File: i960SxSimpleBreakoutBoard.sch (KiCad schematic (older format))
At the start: 26 parts, among them J1 Conn_01x07, J2 Pure Input Pins, J3 Clock, Power, and Bidirection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, J4 Conn_01x05, J5 Multiplexed Address/Data Lines, J6 Upper 16 Address Lines, U1 80960Sx

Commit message: go with a single 1 row connector for the right side of the design
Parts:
- removed J2: Pure Input Pins, Connector_PinHeader_2.54mm:PinHeader_2x03_P2.54mm_Vertical, symbol Connector_Generic:Conn_02x03_Counter_Clockwise
- added J?: Conn_01x11, symbol Connector_Generic:Conn_01x11
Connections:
- net HOLD: now also J?.2 (Pin_2)
- net INT1: now also J?.5 (Pin_5)
- net INT2: now also J?.4 (Pin_4)
- net ~INT0: now also J?.6 (Pin_6)
- net ~INT3: now also J?.3 (Pin_3); no longer J3.5 (Pin_5)
- net ~READY: now also J?.1 (Pin_1)
- net ~RESET: now also J?.7 (Pin_7)
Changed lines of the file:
@@
 Wire Wire Line
 	10650 3450 10950 3450
-Text Label 10950 3550 0    50   ~ 0
+Text Label 11450 2100 0    50   ~ 0
 ~INT3
 Text Label 10950 3450 0    50   ~ 0
@@
 ALE
 Wire Wire Line
-	9600 2400 10100 2400
-Wire Wire Line
-	9600 2500 10100 2500
-Text Label 9600 2400 0    50   ~ 0
+	11450 1900 11950 1900
+Wire Wire Line
+	11450 2000 11950 2000
+Text Label 11450 1900 0    50   ~ 0
 ~READY
 Text Label 6550 4100 0    50   ~ 0
@@
 Text Label 6600 4200 0    50   ~ 0
 HOLD
-Text Label 9600 2500 0    50   ~ 0
+Text Label 11450 2000 0    50   ~ 0
 HOLD
 Wire Wire Line
@@
 Text Label 8200 4500 0    50   ~ 0
 ~RESET
-Text Label 9600 2600 0    50   ~ 0
+Text Label 11450 2500 0    50   ~ 0
 ~RESET
 Wire Wire Line
-	9600 2600 10100 2600
-Text Label 11100 2600 2    50   ~ 0
+	11450 2500 11950 2500
+Text Label 11450 2400 0    50   ~ 0
 ~INT0
-Text Label 11100 2500 2    50   ~ 0
+Text Label 11450 2300 0    50   ~ 0
 INT1
-Text Label 11100 2400 2    50   ~ 0
+Text Label 11450 2200 0    50   ~ 0
 INT2
 Wire Wire Line
-	11100 2600 10600 2600
-Wire Wire Line
-	11100 2500 10600 2500
-Wire Wire Line
-	11100 2400 10600 2400
+	11450 2400 11950 2400
+Wire Wire Line
+	11450 2300 11950 2300
+Wire Wire Line
+	11450 2200 11950 2200
 $Comp
 L power:GND #PWR08
@@
 Wire Wire Line
 	10350 5550 10850 5550
-$Comp
-L Connector_Generic:Conn_02x03_Counter_Clockwise J2
-U 1 1 60272919
-P 10300 2500
-F 0 "J2" H 10350 2817 50  0000 C CNN
-F 1 "Pure Input Pins" H 10350 2726 50  0000 C CNN
-F 2 "Connector_PinHeader_2.54mm:PinHeader_2x03_P2.54mm_Vertical" H 10300 2500 50  0001 C CNN
-F 3 "~" H 10300 2500 50  0001 C CNN
-	1    10300 2500
-	1    0    0    -1
-$EndComp
 $Comp
 L Connector_Generic:Conn_02x03_Counter_Clockwise J3
@@
 $EndComp
 NoConn ~ 13950 3500
+$Comp
+L Connector_Generic:Conn_01x11 J?
+U 1 1 5FBBE5ED
+P 12150 2400
+F 0 "J?" H 12230 2442 50  0000 L CNN
+F 1 "Conn_01x11" H 12230 2351 50  0000 L CNN
+F 2 "" H 12150 2400 50  0001 C CNN
+F 3 "~" H 12150 2400 50  0001 C CNN
+	1    12150 2400
+	1    0    0    -1
+$EndComp
+Wire Wire Line
+	11450 2100 11950 2100
 $EndSCHEMATC

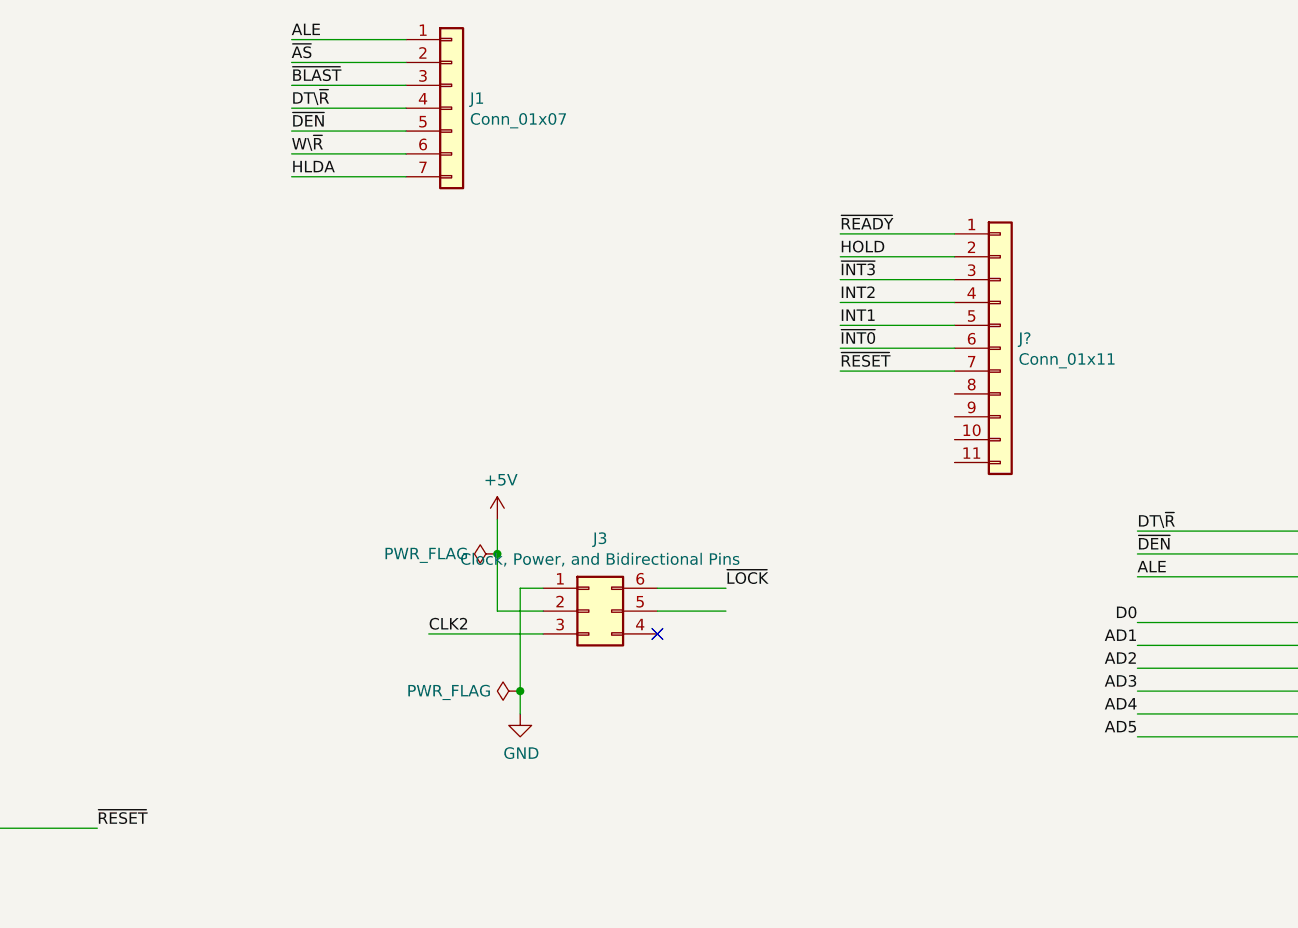
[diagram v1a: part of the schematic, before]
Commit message: Shrunk the size of the final pcb
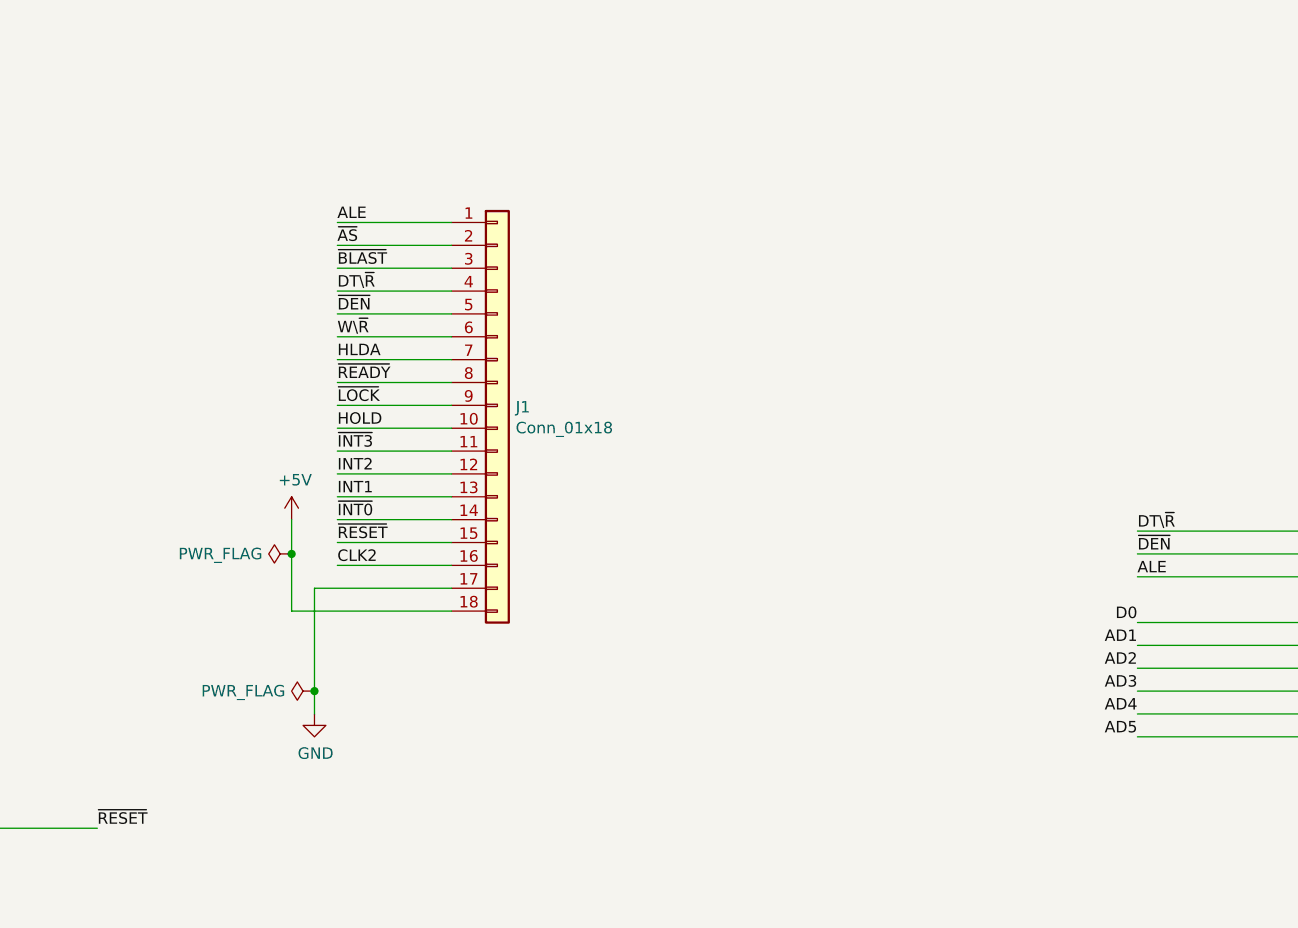
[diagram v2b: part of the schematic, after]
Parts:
- removed J1: Conn_01x07, Connector_PinHeader_2.54mm:PinHeader_1x07_P2.54mm_Vertical, symbol Connector_Generic:Conn_01x07
- removed J3: Clock, Power, and Bidirectional Pins, Connector_PinHeader_2.54mm:PinHeader_2x03_P2.54mm_Vertical, symbol Connector_Generic:Conn_02x03_Counter_Clockwise
- removed J?: Conn_01x11, symbol Connector_Generic:Conn_01x11
- added J1: Conn_01x18, Connector_PinHeader_2.54mm:PinHeader_1x18_P2.54mm_Vertical, symbol Connector_Generic:Conn_01x18
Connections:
- net +5V: now also J1.18 (Pin_18)
- net ALE: now also J1.1 (Pin_1)
- net CLK2: now also J1.16 (Pin_16)
- net DT\~R: now also J1.4 (Pin_4)
- net GND: now also J1.17 (Pin_17)
- net HLDA: now also J1.7 (Pin_7)
- net HOLD: now also J1.10 (Pin_10)
- net INT1: now also J1.13 (Pin_13)
- net INT2: now also J1.12 (Pin_12)
- net W\~R: now also J1.6 (Pin_6)
- net ~AS: now also J1.2 (Pin_2)
- net ~BLAST: now also J1.3 (Pin_3)
- net ~DEN: now also J1.5 (Pin_5)
- net ~INT0: now also J1.14 (Pin_14)
- net ~INT3: now also J1.11 (Pin_11)
- net ~LOCK: now also J1.9 (Pin_9)
- net ~READY: now also J1.8 (Pin_8)
- net ~RESET: now also J1.15 (Pin_15)
- no-connect marks 2 -> 1
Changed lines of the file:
@@
 BA1
 Wire Wire Line
-	9550 1550 9050 1550
-Wire Wire Line
-	9550 1250 9050 1250
-Wire Wire Line
-	9550 1350 9050 1350
-Wire Wire Line
-	9550 1450 9050 1450
-Text Label 9050 1250 0    50   ~ 0
+	9750 2350 9250 2350
+Wire Wire Line
+	9750 2050 9250 2050
+Wire Wire Line
+	9750 2150 9250 2150
+Wire Wire Line
+	9750 2250 9250 2250
+Text Label 9250 2050 0    50   ~ 0
 ~BLAST
-Text Label 9050 1650 0    50   ~ 0
+Text Label 9250 2450 0    50   ~ 0
 HLDA
 Wire Wire Line
@@
 	10350 5450 10850 5450
 Wire Wire Line
-	9050 1650 9550 1650
-Text Label 9050 1550 0    50   ~ 0
+	9250 2450 9750 2450
+Text Label 9250 2350 0    50   ~ 0
 W\~R
 Text Label 4400 5100 2    50   ~ 0
@@
 Text Label 6950 4650 0    50   ~ 0
 ~DEN
-Text Label 9050 1350 0    50   ~ 0
+Text Label 9250 2150 0    50   ~ 0
 DT\~R
-Text Label 9050 1450 0    50   ~ 0
+Text Label 9250 2250 0    50   ~ 0
 ~DEN
 Text Label 6650 4300 0    50   ~ 0
 HLDA
-Wire Wire Line
-	10650 3550 10950 3550
-Wire Wire Line
-	10650 3450 10950 3450
-Text Label 11450 2100 0    50   ~ 0
+Text Label 9250 2850 0    50   ~ 0
 ~INT3
-Text Label 10950 3450 0    50   ~ 0
+Text Label 9250 2650 0    50   ~ 0
 ~LOCK
 Text Label 7300 5050 0    50   ~ 0
@@
 INT2
 Wire Wire Line
-	9050 1050 9550 1050
-Wire Wire Line
-	9050 1150 9550 1150
-Text Label 9050 1050 0    50   ~ 0
+	9250 1850 9750 1850
+Wire Wire Line
+	9250 1950 9750 1950
+Text Label 9250 1850 0    50   ~ 0
 ALE
-Text Label 9050 1150 0    50   ~ 0
+Text Label 9250 1950 0    50   ~ 0
 ~AS
 Text Label 6550 3900 0    50   ~ 0
@@
 ALE
 Wire Wire Line
-	11450 1900 11950 1900
-Wire Wire Line
-	11450 2000 11950 2000
-Text Label 11450 1900 0    50   ~ 0
+	9250 2550 9750 2550
+Wire Wire Line
+	9250 2750 9750 2750
+Text Label 9250 2550 0    50   ~ 0
 ~READY
 Text Label 6550 4100 0    50   ~ 0
@@
 Text Label 6600 4200 0    50   ~ 0
 HOLD
-Text Label 11450 2000 0    50   ~ 0
+Text Label 9250 2750 0    50   ~ 0
 HOLD
 Wire Wire Line
-	9650 3650 10150 3650
-Text Label 9650 3650 0    50   ~ 0
+	9250 3350 9750 3350
+Text Label 9250 3350 0    50   ~ 0
 CLK2
 Text Label 6550 4400 0    50   ~ 0
@@
 Text Label 8200 4500 0    50   ~ 0
 ~RESET
-Text Label 11450 2500 0    50   ~ 0
+Text Label 9250 3250 0    50   ~ 0
 ~RESET
 Wire Wire Line
-	11450 2500 11950 2500
-Text Label 11450 2400 0    50   ~ 0
+	9250 3250 9750 3250
+Text Label 9250 3150 0    50   ~ 0
 ~INT0
-Text Label 11450 2300 0    50   ~ 0
+Text Label 9250 3050 0    50   ~ 0
 INT1
-Text Label 11450 2200 0    50   ~ 0
+Text Label 9250 2950 0    50   ~ 0
 INT2
 Wire Wire Line
-	11450 2400 11950 2400
-Wire Wire Line
-	11450 2300 11950 2300
-Wire Wire Line
-	11450 2200 11950 2200
+	9250 3150 9750 3150
+Wire Wire Line
+	9250 3050 9750 3050
+Wire Wire Line
+	9250 2950 9750 2950
 $Comp
 L power:GND #PWR08
 U 1 1 5FE9A25E
-P 10050 4000
-F 0 "#PWR08" H 10050 3750 50  0001 C CNN
-F 1 "GND" H 10055 3827 50  0000 C CNN
-F 2 "" H 10050 4000 50  0001 C CNN
-F 3 "" H 10050 4000 50  0001 C CNN
-	1    10050 4000
-	1    0    0    -1
-$EndComp
-Wire Wire Line
-	10050 4000 10050 3900
-Wire Wire Line
-	10050 3450 10150 3450
-Wire Wire Line
-	10150 3550 9950 3550
-Wire Wire Line
-	9950 3550 9950 3300
+P 9150 4000
+F 0 "#PWR08" H 9150 3750 50  0001 C CNN
+F 1 "GND" H 9155 3827 50  0000 C CNN
+F 2 "" H 9150 4000 50  0001 C CNN
+F 3 "" H 9150 4000 50  0001 C CNN
+	1    9150 4000
+	1    0    0    -1
+$EndComp
+Wire Wire Line
+	9150 4000 9150 3900
+Wire Wire Line
+	9050 3550 9050 3300
 $Comp
 L power:+5V #PWR07
 U 1 1 5FEDDBF5
-P 9950 3150
-F 0 "#PWR07" H 9950 3000 50  0001 C CNN
-F 1 "+5V" H 9965 3323 50  0000 C CNN
-F 2 "" H 9950 3150 50  0001 C CNN
-F 3 "" H 9950 3150 50  0001 C CNN
-	1    9950 3150
+P 9050 3150
+F 0 "#PWR07" H 9050 3000 50  0001 C CNN
+F 1 "+5V" H 9065 3323 50  0000 C CNN
+F 2 "" H 9050 3150 50  0001 C CNN
+F 3 "" H 9050 3150 50  0001 C CNN
+	1    9050 3150
 	1    0    0    -1
 $EndComp
@@
 L power:PWR_FLAG #FLG01
 U 1 1 5FEDE504
-P 9950 3300
-F 0 "#FLG01" H 9950 3375 50  0001 C CNN
-F 1 "PWR_FLAG" V 9950 3427 50  0000 L CNN
-F 2 "" H 9950 3300 50  0001 C CNN
-F 3 "~" H 9950 3300 50  0001 C CNN
-	1    9950 3300
+P 9050 3300
+F 0 "#FLG01" H 9050 3375 50  0001 C CNN
+F 1 "PWR_FLAG" V 9050 3427 50  0000 L CNN
+F 2 "" H 9050 3300 50  0001 C CNN
+F 3 "~" H 9050 3300 50  0001 C CNN
+	1    9050 3300
 	0    -1   -1   0
 $EndComp
-Connection ~ 9950 3300
-Wire Wire Line
-	9950 3300 9950 3150
+Connection ~ 9050 3300
+Wire Wire Line
+	9050 3300 9050 3150
 $Comp
 L power:PWR_FLAG #FLG02
 U 1 1 5FEDEB67
-P 10050 3900
-F 0 "#FLG02" H 10050 3975 50  0001 C CNN
-F 1 "PWR_FLAG" V 10050 4027 50  0000 L CNN
-F 2 "" H 10050 3900 50  0001 C CNN
-F 3 "~" H 10050 3900 50  0001 C CNN
-	1    10050 3900
+P 9150 3900
+F 0 "#FLG02" H 9150 3975 50  0001 C CNN
+F 1 "PWR_FLAG" V 9150 4027 50  0000 L CNN
+F 2 "" H 9150 3900 50  0001 C CNN
+F 3 "~" H 9150 3900 50  0001 C CNN
+	1    9150 3900
 	0    -1   -1   0
 $EndComp
-Connection ~ 10050 3900
+Connection ~ 9150 3900
 $Comp
 L mechanical:Mounting_Hole MK1
@@
 D0
 Wire Wire Line
-	10050 3450 10050 3900
+	9150 3450 9150 3900
 Wire Wire Line
 	13950 3400 12750 3400
@@
 Wire Wire Line
 	10350 5550 10850 5550
-$Comp
-L Connector_Generic:Conn_02x03_Counter_Clockwise J3
-U 1 1 6028FA37
-P 10350 3550
-F 0 "J3" H 10400 3867 50  0000 C CNN
-F 1 "Clock, Power, and Bidirectional Pins" H 10400 3776 50  0000 C CNN
-F 2 "Connector_PinHeader_2.54mm:PinHeader_2x03_P2.54mm_Vertical" H 10350 3550 50  0001 C CNN
-F 3 "~" H 10350 3550 50  0001 C CNN
-	1    10350 3550
-	1    0    0    -1
-$EndComp
-NoConn ~ 10650 3650
-$Comp
-L Connector_Generic:Conn_01x07 J1
-U 1 1 5F82ACA9
-P 9750 1350
-F 0 "J1" H 9830 1392 50  0000 L CNN
-F 1 "Conn_01x07" H 9830 1301 50  0000 L CNN
-F 2 "Connector_PinHeader_2.54mm:PinHeader_1x07_P2.54mm_Vertical" H 9750 1350 50  0001 C CNN
-F 3 "~" H 9750 1350 50  0001 C CNN
-	1    9750 1350
-	1    0    0    -1
-$EndComp
 $Comp
 L Connector_Generic:Conn_01x05 J4
@@
 $EndComp
 NoConn ~ 13950 3500
-$Comp
-L Connector_Generic:Conn_01x11 J?
-U 1 1 5FBBE5ED
-P 12150 2400
-F 0 "J?" H 12230 2442 50  0000 L CNN
-F 1 "Conn_01x11" H 12230 2351 50  0000 L CNN
-F 2 "" H 12150 2400 50  0001 C CNN
-F 3 "~" H 12150 2400 50  0001 C CNN
-	1    12150 2400
-	1    0    0    -1
-$EndComp
-Wire Wire Line
-	11450 2100 11950 2100
+Wire Wire Line
+	9250 2850 9750 2850
+Wire Wire Line
+	9250 2650 9750 2650
+Wire Wire Line
+	9150 3450 9750 3450
+Wire Wire Line
+	9050 3550 9750 3550
+$Comp
+L Connector_Generic:Conn_01x18 J1
+U 1 1 5FC8EA14
+P 9950 2650
+F 0 "J1" H 10030 2642 50  0000 L CNN
+F 1 "Conn_01x18" H 10030 2551 50  0000 L CNN
+F 2 "Connector_PinHeader_2.54mm:PinHeader_1x18_P2.54mm_Vertical" H 9950 2650 50  0001 C CNN
+F 3 "~" H 9950 2650 50  0001 C CNN
+	1    9950 2650
+	1    0    0    -1
+$EndComp
 $EndSCHEMATC
